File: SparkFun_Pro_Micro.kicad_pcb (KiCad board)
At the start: 2 copper layers, 17.8 x 34.5 mm, 32 parts, among them P1 USB_C_Plug, U2 MIC5219, U3 ATMEGA32U4, Y1 16MHz

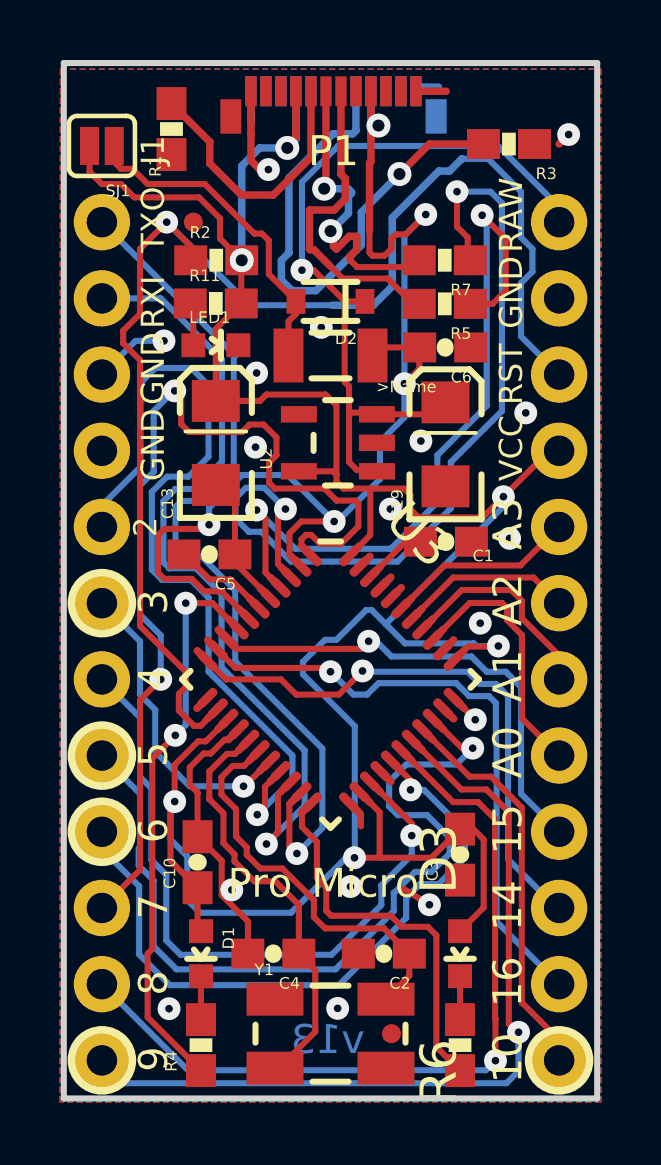
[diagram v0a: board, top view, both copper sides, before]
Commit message: remove old pro micro schetches
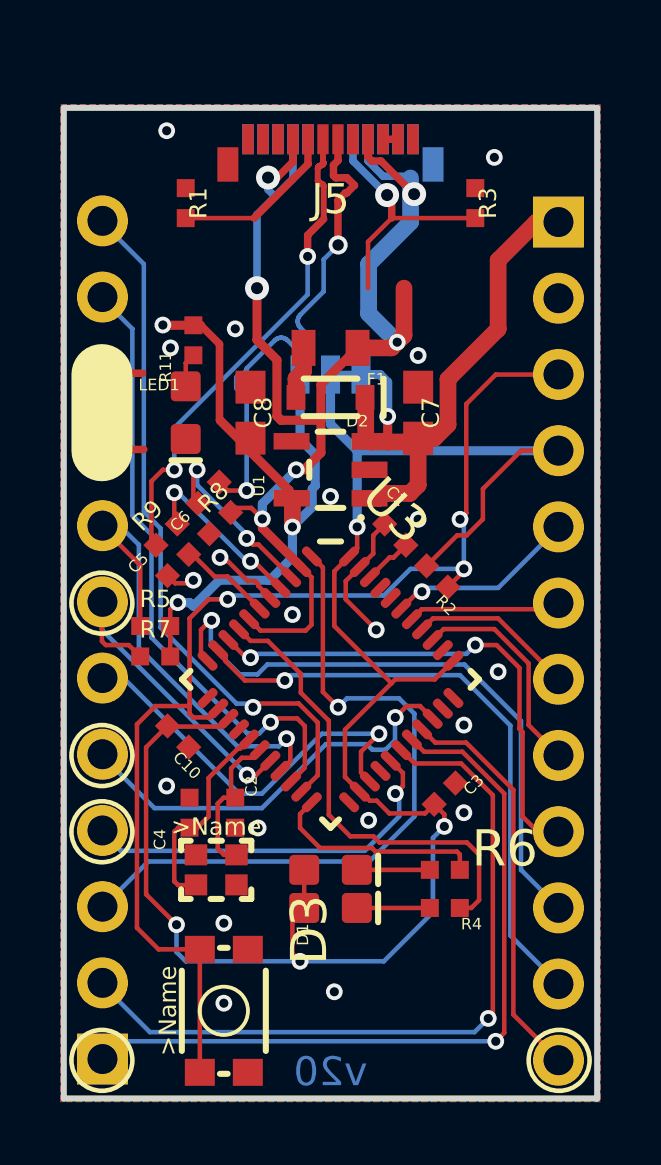
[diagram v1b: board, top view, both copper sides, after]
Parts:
- removed C13, C19: 10uF, SparkFun_Pro_Micro:EIA3216
- removed JP1, JP2: FIDUCIALUFIDUCIAL, SparkFun_Pro_Micro:MICRO-FIDUCIAL
- removed JP6, JP7: M12PTH, SparkFun_Pro_Micro:1X12
- removed P1: USB_C_Plug, Connector_USB:USB_C_Plug_Molex_105444
- removed SJ1: Closed for 5V Board, SparkFun_Pro_Micro:SJ_2S
- removed U2: MIC5219, SparkFun_Pro_Micro:SOT23-5
- removed Y1: 16MHz, SparkFun_Pro_Micro:CRYSTAL-SMD-5X3
- added C7: 10uF, SparkFun_Pro_Micro:0603, F.Cu at (151.4, 98.7)
- added C8: 10uF, SparkFun_Pro_Micro:0603, F.Cu at (145.8, 98.7)
- added J3: CONN_12CASTLE, Connector_PinSocket_2.54mm:PinSocket_1x12_P2.54mm_Vertical, B.Cu at (140.9, 120.2)
- added J4: CONN_12CASTLE, Connector_PinSocket_2.54mm:PinSocket_1x12_P2.54mm_Vertical, B.Cu at (156.1, 92.3)
- added J5: USB_C5, Connector_USB:USB_C_Plug_Molex_105444, F.Cu at (148.5, 89.5)
- added JP4: JUMPER-SMT_3_1-NC_TRACE_SILK, SparkFun_Pro_Micro:SMT-JUMPER_3_1-NC_TRACE_SILK, B.Cu at (148.5, 97.4)
- added LOGO5: SPECIAL_INSTRUCTIONS-ORDERING, SparkFun_Pro_Micro:ORDERING_INSTRUCTIONS, F.Cu at (162.5, 70.7)
- added R8: 22OHM-0402T-1/16W-1%, SparkFun_Pro_Micro:0402-TIGHT, F.Cu at (144.4, 101.3)
- added R9: 22OHM-0402T-1/16W-1%, SparkFun_Pro_Micro:0402-TIGHT, F.Cu at (143.0, 102.7)
- added S1: Reset, SparkFun_Pro_Micro:TACTILE_SWITCH_SMD_4.6X2.8MM, F.Cu at (144.9, 118.6)
- added U$3: OSHW-LOGOMINI, SparkFun_Pro_Micro:OSHW-LOGO-MINI, B.Cu at (155.9, 90.0)
- added U1: 3.3V, SparkFun_Pro_Micro:SOT23-5, F.Cu at (148.5, 100.6)
- added Y2: 16MHz, SparkFun_Pro_Micro:CRYSTAL-SMD-2.0X1.6MM, F.Cu at (144.7, 113.9)
- C1, C2, C3, C4: footprint SparkFun_Pro_Micro:0603-CAP -> SparkFun_Pro_Micro:0402-TIGHT
- C10, C5, C6: value 1uF -> 1.0uF; footprint SparkFun_Pro_Micro:0603-CAP -> SparkFun_Pro_Micro:0402-TIGHT
- D2: value DIODESOD -> 3A/10V/280mV
- D3: value Green -> GREEN
- F1: value 500mA -> 6V 0.5A; footprint SparkFun_Pro_Micro:PTC-1206 -> SparkFun_Pro_Micro:0805
- LED1: value Red -> RED
- R1, R3: value 22 -> 5.1k; footprint SparkFun_Pro_Micro:0603-RES -> SparkFun_Pro_Micro:0402-TIGHT
- R11: value 1K -> 1k; footprint SparkFun_Pro_Micro:0603-RES -> SparkFun_Pro_Micro:0402-TIGHT
- R2: value 10K -> 10k; footprint SparkFun_Pro_Micro:0603-RES -> SparkFun_Pro_Micro:0402-TIGHT
- R4, R6: value 330 -> 1k; footprint SparkFun_Pro_Micro:0603-RES -> SparkFun_Pro_Micro:0402-TIGHT
- R5, R7: value 22 -> 2.2k; footprint SparkFun_Pro_Micro:0603-RES -> SparkFun_Pro_Micro:0402-TIGHT
- U3: value ATMEGA32U4 -> 32U4; footprint SparkFun_Pro_Micro:QFN-44-NOPAD_1_1-OUTFAKES -> SparkFun_Pro_Micro:QFN-44-NOPAD_1_1-LESS_PASTE
- moved FRAME1 27.8 mm to (145.8, 64.9)
- moved R7 16.4 mm to (142.7, 106.8), turned to 0 degrees
- moved R5 14.4 mm to (142.7, 105.8), turned to 0 degrees
- moved R2 12.9 mm to (152.1, 104.1), turned to 135 degrees
- moved C6 9.52 mm to (144.8, 102.3), turned to 45 degrees
- moved R4 9.33 mm to (152.3, 115.2), turned to 180 degrees
- moved C2 6.83 mm to (145.3, 112.0), turned to 270 degrees
- moved R6 5.86 mm to (152.3, 113.9), turned to 180 degrees
- moved C4 5.47 mm to (143.8, 112.0), turned to 90 degrees
- moved D3 5.14 mm to (148.5, 113.9), turned to 0 degrees
- moved D1 4.58 mm to (148.5, 115.2), turned to 0 degrees
- moved C10 4.24 mm to (143.4, 109.4), turned to 135 degrees
- moved D2 3.20 mm to (148.5, 98.1)
- moved R1 2.51 mm to (143.7, 91.7), turned to 270 degrees
- moved LED1 2.46 mm to (143.7, 98.7)
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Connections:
- net /D14 renamed Net-(R4-Pad1)
- net Net-(C5-Pad2) renamed /UCAP
- C10 pad 1: 3.3V -> GND
- C10 pad 2: GND -> VCC
- C3 pad 2: 3.3V -> VCC
- C6 pad 2: 3.3V -> V_USB
- D1 pad A: 3.3V -> VCC
- D3 pad A: 3.3V -> VCC
- F1 pad 1: 3.3V -> V_USB
- F1 pad 2: Net-(D2-Pad2) -> Net-(D2-PadA)
- R2 pad 2: 3.3V -> VCC
- R5 pad 1: /D- -> /D2/SDA
- R5 pad 2: /D- -> 3.3V
- R7 pad 1: /D+ -> /D3/SCL
- R7 pad 2: /D+ -> 3.3V
- U3 pad 14: 3.3V -> VCC
- U3 pad 18: /D3 -> /D3/SCL
- U3 pad 19: /D2 -> /D2/SDA
- U3 pad 2: 3.3V -> V_USB
- U3 pad 24: 3.3V -> VCC
- U3 pad 34: 3.3V -> VCC
- U3 pad 44: 3.3V -> VCC
- U3 pad 7: 3.3V -> V_USB
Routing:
- net 3.3V: track 132.0 -> 23.2 mm, vias 11 -> 3
- net VCC: track 0.00 -> 61.8 mm, vias 0 -> 4
- net V_USB: track 0.00 -> 43.8 mm, vias 0 -> 6
- net /D+: track 63.8 -> 22.4 mm, vias 6 -> 4
- net /D2: track 27.8 -> 0.00 mm, vias 1 -> 0
- net /D2/SDA: track 0.00 -> 16.4 mm, vias 0 -> 1
- net /D5: track 27.6 -> 13.9 mm
- net /D-: track 10.4 -> 22.6 mm, vias 0 -> 4
- net /D3/SCL: track 0.00 -> 11.5 mm, vias 0 -> 1
- net GND: track 24.2 -> 13.0 mm, vias 17 -> 20
- net Net-(D2-Pad2): track 11.1 -> 0.00 mm
- net /D6: track 23.2 -> 12.8 mm
- net /D3: track 9.86 -> 0.00 mm, vias 1 -> 0
- net /D7: track 32.8 -> 23.4 mm, vias 2 -> 1
- net /D4: track 22.3 -> 13.6 mm
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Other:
- board size 17.8 x 34.5 mm -> 17.8 x 33 mm
- net class Default: clearance 0.1778 -> 0.1016
- rule trace_clearance: 0.1778 -> 0.1016
- rule trace_min: 0.2 -> 0.1524
- rule via_min_drill: 0.254 -> 0.3
- board text added: "0.8mm PCB"
- board text added: "N Seidle"
- board text added: "Units in Inches"
- board text added: "v20"
- board text removed: "10"
- board text removed: "14"
- board text removed: "15"
- board text removed: "16"
- board text removed: "2"
- board text removed: "3"
- board text removed: "3.3V"
- board text removed: "3.3V Reg / 8MHz"
- board text removed: "4"
- board text removed: "5"
- board text removed: "5V"
- board text removed: "5V Reg / 16MHz"
- board text removed: "6"
- board text removed: "7"
- board text removed: "8"
- board text removed: "9"
- board text removed: "A0"
- board text removed: "A1"
- board text removed: "A2"
- board text removed: "A3"
- board text removed: "GND"
- board text removed: "J1"
- board text removed: "Mark back accordingly"
- board text removed: "Micro"
- board text removed: "Pro"
- board text removed: "RAW"
- board text removed: "RST"
- board text removed: "RXI"
- board text removed: "TXO"
- board text removed: "VCC"
- board text removed: "Valid combinations:"
- board text removed: "v13"
